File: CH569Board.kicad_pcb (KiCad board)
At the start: 4 copper layers, 47.3 x 49.6 mm, 37 parts, among them CN1 BA42-80BT-1-NHB, J1 Conn_01x02_Male, J2 Conn_01x03_Male, U1 AMS1117-3.3, U2 AMS1117-1.2, U3 W25Q32JVSSIQ, U4 CH569W, X1 O705030MEEA4SC

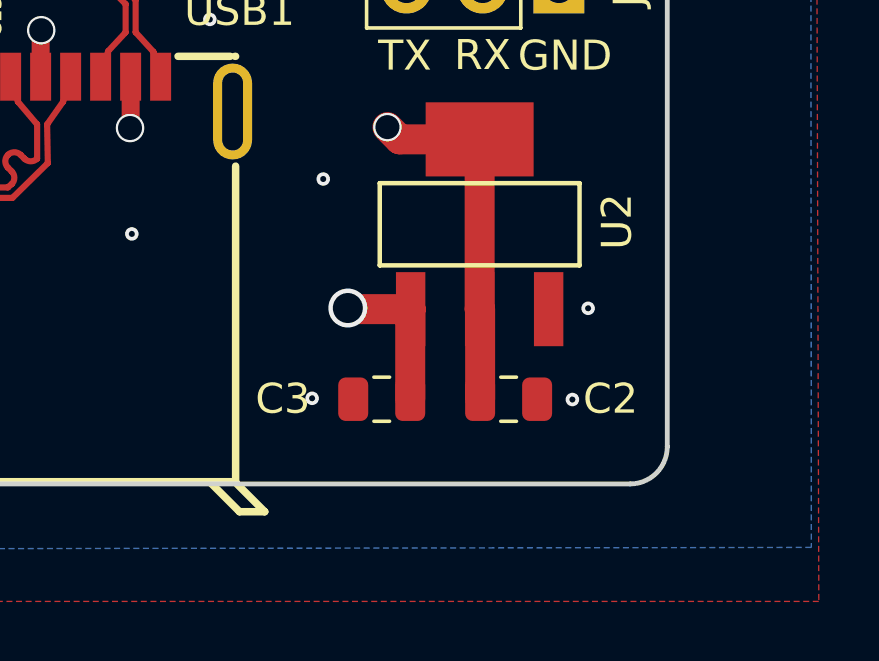
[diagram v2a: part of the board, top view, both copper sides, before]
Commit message: Fix swapped pins 1 and 3 on the 1.2V regulator
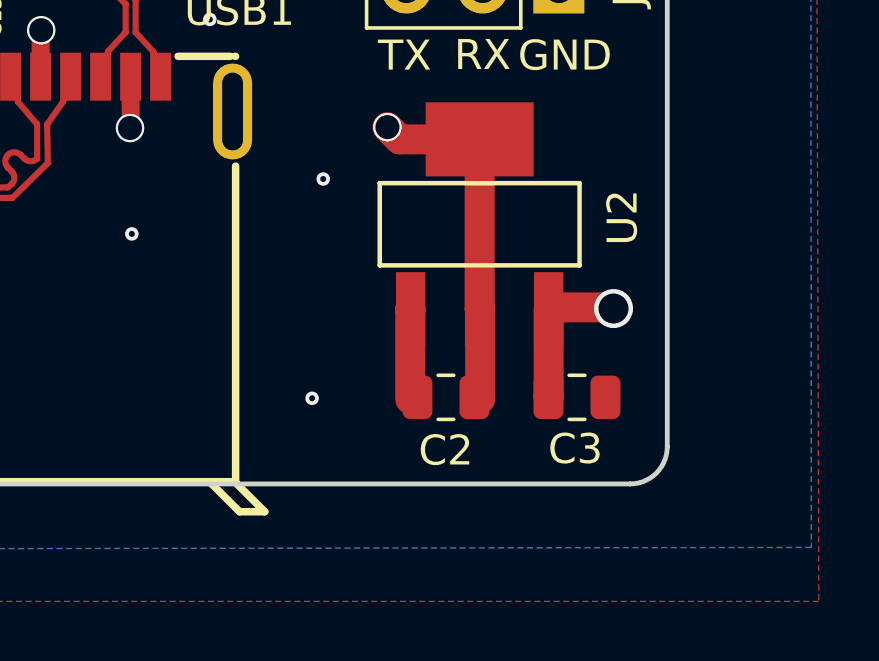
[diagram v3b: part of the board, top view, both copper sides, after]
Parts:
- moved C3 6.51 mm to (144.7, 124.9), turned to 180 degrees
- moved C2 2.09 mm to (140.3, 124.9), turned to 0 degrees
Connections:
- U2 pad 1: +5V -> GND
- U2 pad 3: GND -> +5V
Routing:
- net +5V: track 44.3 -> 54.9 mm
- net GND: track 72.3 -> 75.3 mm, vias 76 -> 74
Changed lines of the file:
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@@
   )
   (footprint "Capacitor_SMD:C_0805_2012Metric" (layer "F.Cu")
-    (at 138.17 124.98)
+    (at 144.6784 124.9172 180)
     (descr "Capacitor SMD 0805 (2012 Metric), square (rectangular) end terminal, IPC_7351 nominal, (Body size source: IPC-SM-782 page 76, https://www.pcb-3d.com/wordpress/wp-content/uploads/ipc-sm-782a_amendment_1_and_2.pdf, https://docs.google.com/spreadsheets/d/1BsfQQcO9C6DZCsRaXUlFlo91Tg2WpOkGARC1WS5S8t0/edit?usp=sharing), generated with kicad-footprint-generator")
     (tags "capacitor")
@@
     (property "Sheetname" "")
     (attr smd)
-    (fp_text reference "C3" (at -3.296 -0.012) (layer "F.SilkS")
+    (fp_text reference "C3" (at 0.0508 -1.7272) (layer "F.SilkS")
       (effects (font (size 1 1) (thickness 0.15)))
     )
@@
     (fp_line (start -1 -0.625) (end 1 -0.625) (layer "F.Fab") (width 0.1))
     (fp_line (start 1 0.625) (end -1 0.625) (layer "F.Fab") (width 0.1))
-    (pad "1" smd roundrect (at -0.95 0) (size 1 1.45) (layers "F.Cu" "F.Paste" "F.Mask") (roundrect_rratio 0.25)
+    (pad "1" smd roundrect (at -0.95 0 180) (size 1 1.45) (layers "F.Cu" "F.Paste" "F.Mask") (roundrect_rratio 0.25)
       (net 1 "GND") (pintype "passive"))
-    (pad "2" smd roundrect (at 0.95 0) (size 1 1.45) (layers "F.Cu" "F.Paste" "F.Mask") (roundrect_rratio 0.25)
+    (pad "2" smd roundrect (at 0.95 0 180) (size 1 1.45) (layers "F.Cu" "F.Paste" "F.Mask") (roundrect_rratio 0.25)
       (net 3 "+5V") (pintype "passive"))
     (model "${KICAD6_3DMODEL_DIR}/Capacitor_SMD.3dshapes/C_0805_2012Metric.wrl"
@@
   )
   (footprint "Capacitor_SMD:C_0805_2012Metric" (layer "F.Cu")
-    (at 142.4 124.98 180)
+    (at 140.3096 124.9172)
     (descr "Capacitor SMD 0805 (2012 Metric), square (rectangular) end terminal, IPC_7351 nominal, (Body size source: IPC-SM-782 page 76, https://www.pcb-3d.com/wordpress/wp-content/uploads/ipc-sm-782a_amendment_1_and_2.pdf, https://docs.google.com/spreadsheets/d/1BsfQQcO9C6DZCsRaXUlFlo91Tg2WpOkGARC1WS5S8t0/edit?usp=sharing), generated with kicad-footprint-generator")
     (tags "capacitor")
@@
     (property "Sheetname" "")
     (attr smd)
-    (fp_text reference "C2" (at -3.396 0.012 180) (layer "F.SilkS")
-      (effects (font (size 1 1) (thickness 0.15)))
-    )
-    (fp_text value "100n" (at 0 1.68 180) (layer "F.Fab")
-      (effects (font (size 1 1) (thickness 0.15)))
-    )
-    (fp_text user "${REFERENCE}" (at 0 0 180) (layer "F.Fab")
+    (fp_text reference "C2" (at 0 1.778) (layer "F.SilkS")
+      (effects (font (size 1 1) (thickness 0.15)))
+    )
+    (fp_text value "100n" (at 0 1.68) (layer "F.Fab")
+      (effects (font (size 1 1) (thickness 0.15)))
+    )
+    (fp_text user "${REFERENCE}" (at 0 0) (layer "F.Fab")
       (effects (font (size 0.5 0.5) (thickness 0.08)))
     )
@@
     (fp_line (start -1 0.625) (end -1 -0.625) (layer "F.Fab") (width 0.1))
     (fp_line (start -1 -0.625) (end 1 -0.625) (layer "F.Fab") (width 0.1))
-    (pad "1" smd roundrect (at -0.95 0 180) (size 1 1.45) (layers "F.Cu" "F.Paste" "F.Mask") (roundrect_rratio 0.25)
+    (pad "1" smd roundrect (at -0.95 0) (size 1 1.45) (layers "F.Cu" "F.Paste" "F.Mask") (roundrect_rratio 0.25)
       (net 1 "GND") (pintype "passive"))
-    (pad "2" smd roundrect (at 0.95 0 180) (size 1 1.45) (layers "F.Cu" "F.Paste" "F.Mask") (roundrect_rratio 0.25)
+    (pad "2" smd roundrect (at 0.95 0) (size 1 1.45) (layers "F.Cu" "F.Paste" "F.Mask") (roundrect_rratio 0.25)
       (net 26 "+1V2") (pintype "passive"))
     (model "${KICAD6_3DMODEL_DIR}/Capacitor_SMD.3dshapes/C_0805_2012Metric.wrl"
@@
     (property "Sheetname" "")
     (attr through_hole)
-    (fp_text reference "U2" (at -0.088 -4.576 -90) (layer "F.SilkS")
+    (fp_text reference "U2" (at -0.2252 -4.7684 -90) (layer "F.SilkS")
       (effects (font (size 1 1) (thickness 0.15)))
     )
@@
     )
     (fp_line (start 1.37 3.33) (end -1.37 3.33) (layer "F.SilkS") (width 0.15))
-    (fp_line (start -1.37 3.33) (end -1.37 -3.33) (layer "F.SilkS") (width 0.15))
     (fp_line (start -1.37 -3.33) (end 1.37 -3.33) (layer "F.SilkS") (width 0.15))
     (fp_line (start 1.37 -3.33) (end 1.37 3.33) (layer "F.SilkS") (width 0.15))
+    (fp_line (start -1.37 3.33) (end -1.37 -3.33) (layer "F.SilkS") (width 0.15))
     (fp_circle (center 3.56 2.41) (end 3.81 2.41) (layer "Cmts.User") (width 0.5) (fill none))
     (fp_circle (center 3.5 3.25) (end 3.53 3.25) (layer "F.Fab") (width 0.06) (fill none))
     (pad "1" smd rect locked (at 2.83 2.3 270) (size 2.47 0.98) (layers "F.Cu" "F.Paste" "F.Mask")
-      (net 3 "+5V") (pinfunction "In") (pintype "unspecified"))
+      (net 1 "GND") (pinfunction "GND") (pintype "unspecified"))
     (pad "2" smd rect locked (at 2.83 0 270) (size 2.47 0.98) (layers "F.Cu" "F.Paste" "F.Mask")
       (net 26 "+1V2") (pinfunction "Out") (pintype "unspecified"))
     (pad "3" smd rect locked (at 2.83 -2.3 270) (size 2.47 0.98) (layers "F.Cu" "F.Paste" "F.Mask")
-      (net 1 "GND") (pinfunction "GND") (pintype "unspecified"))
+      (net 3 "+5V") (pinfunction "In") (pintype "unspecified"))
     (pad "4" smd rect locked (at -2.83 0 270) (size 2.47 3.6) (layers "F.Cu" "F.Paste" "F.Mask")
       (net 26 "+1V2") (pinfunction "TAB") (pintype "unspecified"))
@@
   (segment (start 130.82 82.45) (end 130.81 82.44) (width 0.20574) (layer "F.Cu") (net 1))
   (segment (start 102.61 120.68) (end 102.61 120.2) (width 1) (layer "F.Cu") (net 1))
+  (segment (start 139.12 124.98) (end 139.12 121.992) (width 1) (layer "F.Cu") (net 1))
   (segment (start 126.81 84.79) (end 126.81 79.99) (width 0.20574) (layer "F.Cu") (net 1))
   (segment (start 129.8 115.92) (end 129.78 115.94) (width 0.6) (layer "F.Cu") (net 1))
   (segment (start 122.81 84.79) (end 122.81 82.45) (width 0.20574) (layer "F.Cu") (net 1))
   (segment (start 126.8 112.7) (end 126.82 112.68) (width 0.6) (layer "F.Cu") (net 1))
+  (segment (start 139.12 121.992) (end 139.134 121.978) (width 1) (layer "F.Cu") (net 1))
   (segment (start 102.23 119.82) (end 102.23 118.071) (width 1) (layer "F.Cu") (net 1))
   (segment (start 117.076887 104.57) (end 117.023147 104.51626) (width 1) (layer "F.Cu") (net 1))
@@
   (via (at 110.52 126.73) (size 0.45) (drill 0.2) (layers "F.Cu" "B.Cu") (free) (net 1))
   (via (at 126.81 82.46) (size 0.45) (drill 0.2) (layers "F.Cu" "B.Cu") (net 1))
-  (via (at 145.05 121.95) (size 0.45) (drill 0.2) (layers "F.Cu" "B.Cu") (free) (net 1))
   (via (at 117.023147 104.51626) (size 0.95) (drill 0.8) (layers "F.Cu" "B.Cu") (net 1))
   (via (at 127.7112 105.521) (size 0.95) (drill 0.8) (layers "F.Cu" "B.Cu") (net 1))
@@
   (via (at 136.22 117.64) (size 0.45) (drill 0.2) (layers "F.Cu" "B.Cu") (free) (net 1))
   (via (at 125.848191 94.02063) (size 0.75) (drill 0.6) (layers "F.Cu" "B.Cu") (net 1))
-  (via (at 144.525 124.99) (size 0.45) (drill 0.2) (layers "F.Cu" "B.Cu") (free) (net 1))
   (via (at 138.81 82.39) (size 0.45) (drill 0.2) (layers "F.Cu" "B.Cu") (net 1))
   (via (at 101.37 120.69) (size 0.45) (drill 0.2) (layers "F.Cu" "B.Cu") (free) (net 1))
@@
   (segment (start 122.48 104.08) (end 122.11 104.11) (width 0.2) (layer "B.Cu") (net 2))
   (segment (start 106.839 118.062) (end 108.528 118.062) (width 1) (layer "F.Cu") (net 3))
-  (segment (start 139.134 121.978) (end 137.078 121.978) (width 1) (layer "F.Cu") (net 3))
+  (segment (start 143.8028 121.92) (end 145.8588 121.92) (width 1) (layer "F.Cu") (net 3))
   (segment (start 110.4904 118.062) (end 110.505 118.0474) (width 1) (layer "F.Cu") (net 3))
-  (segment (start 139.12 124.98) (end 139.12 121.992) (width 1) (layer "F.Cu") (net 3))
-  (segment (start 137.078 121.978) (end 137.04 121.94) (width 1) (layer "F.Cu") (net 3))
-  (segment (start 139.12 121.992) (end 139.134 121.978) (width 1) (layer "F.Cu") (net 3))
+  (segment (start 143.734 121.978) (end 143.734 124.9116) (width 1) (layer "F.Cu") (net 3))
   (segment (start 110.505 118.0474) (end 110.505 113.0694) (width 1) (layer "F.Cu") (net 3))
+  (segment (start 143.734 124.9116) (end 143.7284 124.9172) (width 1) (layer "F.Cu") (net 3))
   (segment (start 108.528 118.062) (end 110.4904 118.062) (width 1) (layer "F.Cu") (net 3))
   (via (at 108.528 118.062) (size 1.3) (drill 1) (layers "F.Cu" "B.Cu") (net 3))
-  (via (at 137.04 121.94) (size 1.3) (drill 1) (layers "F.Cu" "B.Cu") (net 3))
-  (segment (start 108.528 118.788) (end 111.68 121.94) (width 1) (layer "In2.Cu") (net 3))
+  (via (at 145.8968 121.958) (size 1.3) (drill 1) (layers "F.Cu" "B.Cu") (net 3))
+  (segment (start 108.528 118.062) (end 114.0624 123.5964) (width 1) (layer "In2.Cu") (net 3))
+  (segment (start 114.0624 123.5964) (end 144.5768 123.5964) (width 1) (layer "In2.Cu") (net 3))
   (segment (start 108.528 118.062) (end 108.528 118.788) (width 1) (layer "In2.Cu") (net 3))
-  (segment (start 111.68 121.94) (end 137.04 121.94) (width 1) (layer "In2.Cu") (net 3))
+  (segment (start 145.8968 122.2764) (end 145.8968 121.958) (width 1) (layer "In2.Cu") (net 3))
+  (segment (start 144.5768 123.5964) (end 145.8968 122.2764) (width 1) (layer "In2.Cu") (net 3))
   (segment (start 110.505 121.1974) (end 110.505 123.1938) (width 1) (layer "F.Cu") (net 23))
   (segment (start 110.505 123.1938) (end 110.5304 123.2192) (width 1) (layer "F.Cu") (net 23))

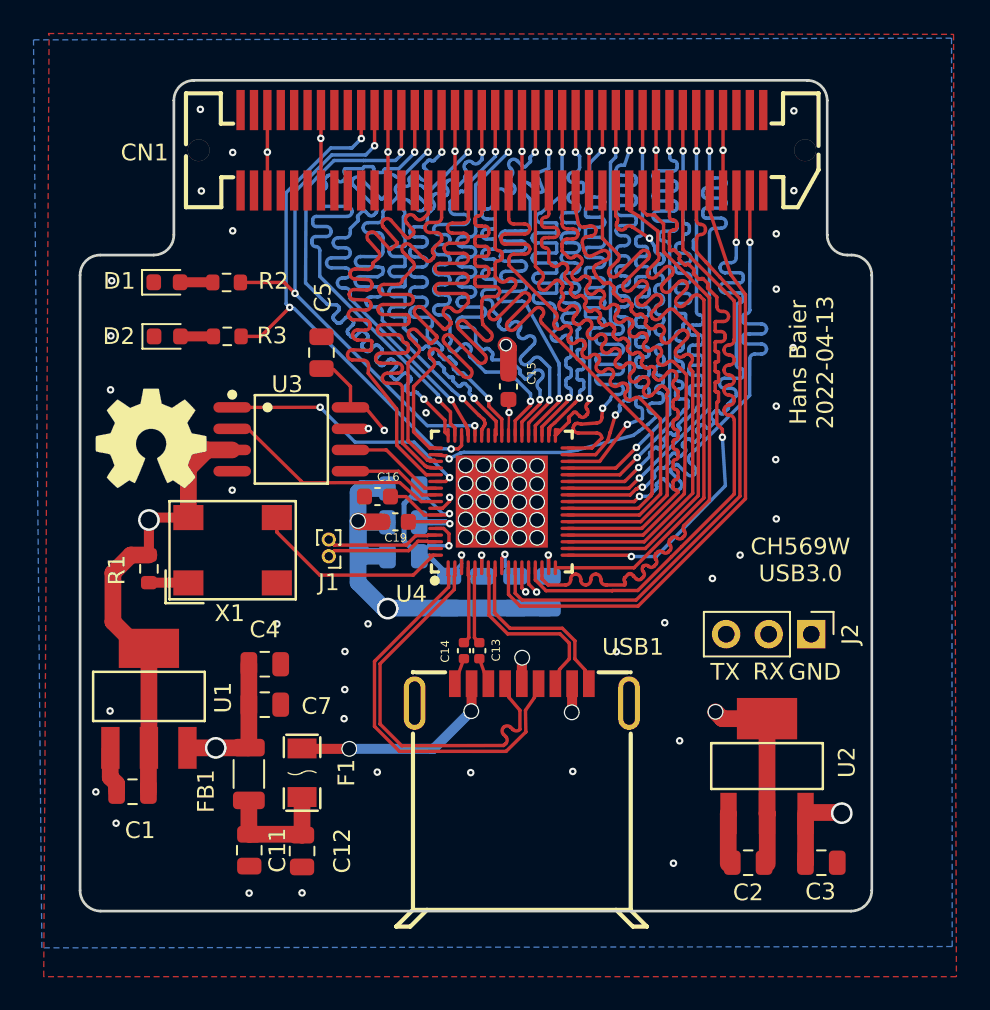
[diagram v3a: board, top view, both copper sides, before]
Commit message: add decoupling caps in serdes, layout improvements
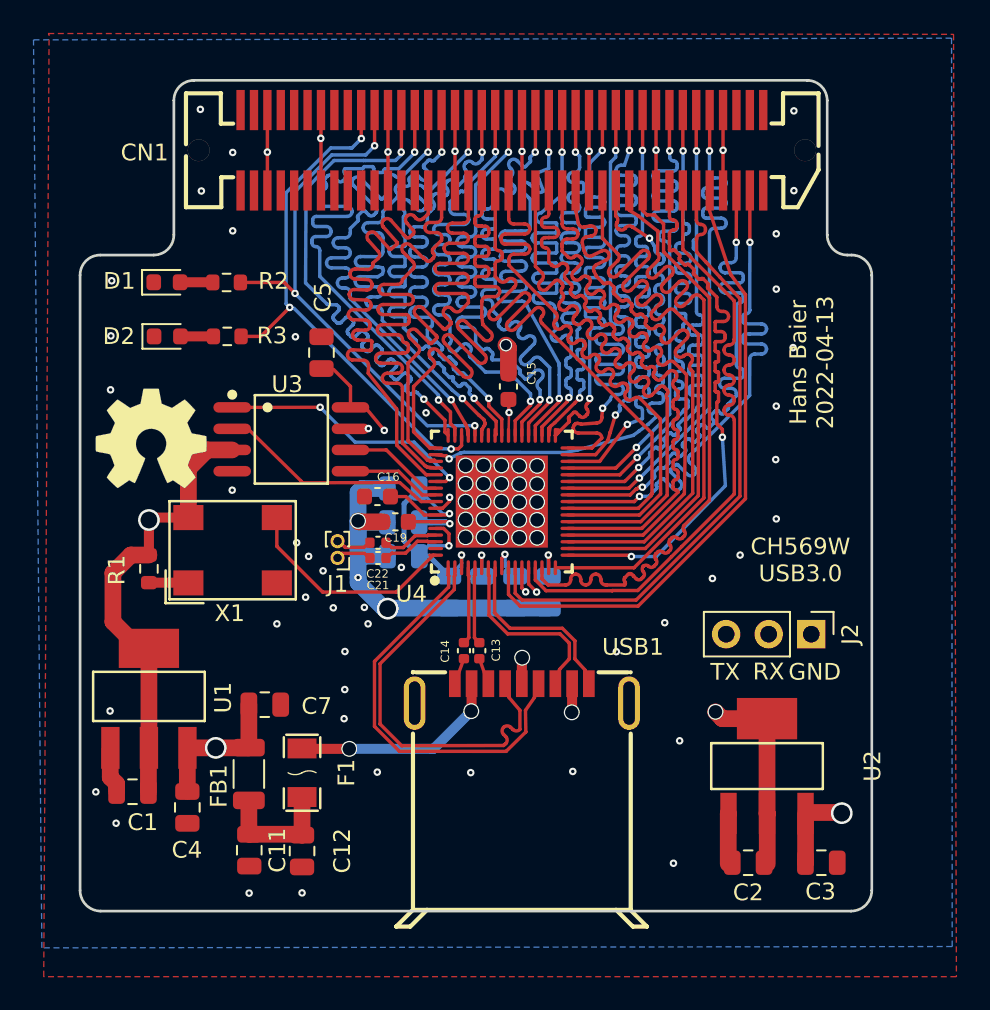
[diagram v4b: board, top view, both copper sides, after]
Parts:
- added C21: 100nF, Capacitor_SMD:C_0402_1005Metric, F.Cu at (118.2, 106.7)
- added C22: 100nF, Capacitor_SMD:C_0402_1005Metric, F.Cu at (118.2, 105.8)
- moved C4 9.72 mm to (106.8, 121.6), turned to 90 degrees
- moved J1 0.53 mm to (115.8, 106.7)
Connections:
- J1 pad 1: /GX+ -> Net-(J1-Pad1)
- J1 pad 2: /GX- -> Net-(J1-Pad2)
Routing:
- net /GX-: track 6.76 -> 3.37 mm
- net /GX+: track 6.76 -> 3.37 mm
- net Net-(J1-Pad2): track 0.00 -> 2.18 mm
- net Net-(J1-Pad1): track 0.00 -> 2.15 mm
- net /XI: track 11.9 -> 13.2 mm
- net GND: vias 74 -> 83
